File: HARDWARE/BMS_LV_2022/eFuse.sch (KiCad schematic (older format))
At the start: 12 parts, among them Q10 BSS138, Q11 SiSS05DN, Q12 SiSS05DN, Q8 SiSS05DN, Q9 SiSS05DN

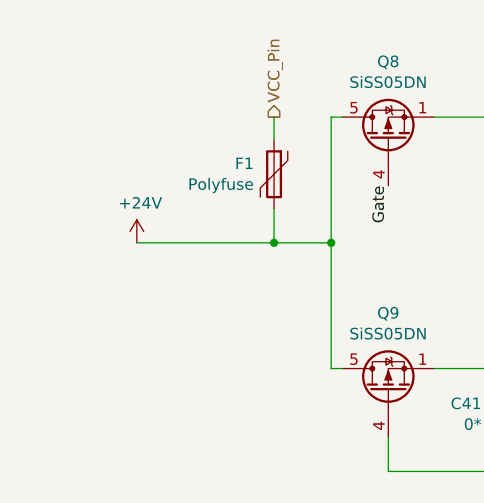
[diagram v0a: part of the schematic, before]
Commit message: PCB Routing Update 2
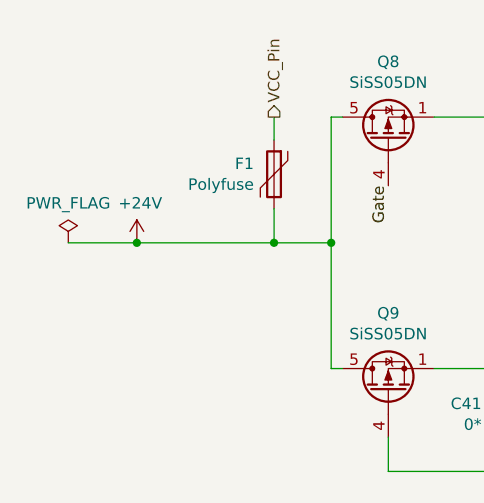
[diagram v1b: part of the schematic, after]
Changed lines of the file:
@@
 Wire Wire Line
 	6050 3350 6050 3450
+$Comp
+L power:PWR_FLAG #FLG0106
+U 1 1 61ECFB96
+P 3950 2800
+F 0 "#FLG0106" H 3950 2875 50  0001 C CNN
+F 1 "PWR_FLAG" H 3950 2973 50  0000 C CNN
+F 2 "" H 3950 2800 50  0001 C CNN
+F 3 "~" H 3950 2800 50  0001 C CNN
+	1    3950 2800
+	1    0    0    -1
+$EndComp
+Wire Wire Line
+	4250 2800 3950 2800
+Connection ~ 4250 2800
 $EndSCHEMATC

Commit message: Changes in V1.0
-Fuse holder change
-Autosport conn angle change
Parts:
- F2: footprint footprints:Fuseholder_Keystone_3522-2 -> footprints:3557-2; Part Number 3522-2 -> 3557-2
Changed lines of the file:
@@
 F 0 "F2" V 6853 2800 50  0000 C CNN
 F 1 "Fuse" V 6944 2800 50  0000 C CNN
-F 2 "footprints:Fuseholder_Keystone_3522-2" V 6980 2800 50  0001 C CNN
+F 2 "footprints:3557-2" V 6980 2800 50  0001 C CNN
 F 3 "~" H 7050 2800 50  0001 C CNN
-F 4 "3522-2" H 7050 2800 50  0001 C CNN "Part Number"
+F 4 "3557-2" H 7050 2800 50  0001 C CNN "Part Number"
 	1    7050 2800
 	0    1    1    0

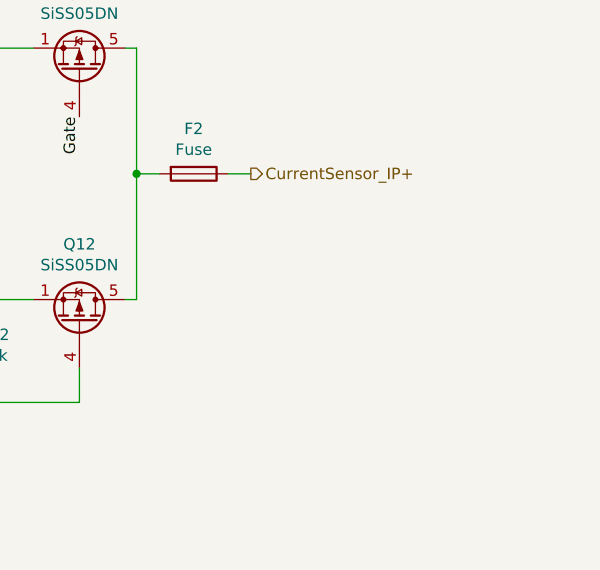
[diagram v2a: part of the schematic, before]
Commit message: Last Changes in V1.0
Fuse voltage measurement added
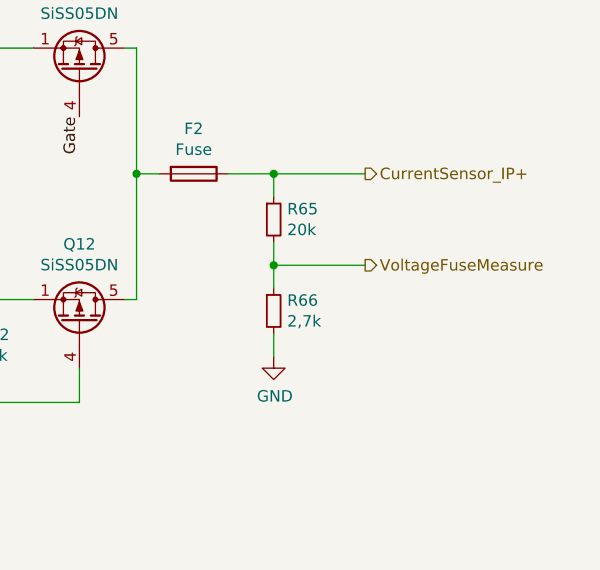
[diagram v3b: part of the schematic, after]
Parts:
- added R65: 20k, Resistor_SMD:R_0603_1608Metric, symbol Device:R_Small
- added R66: 2,7k, Resistor_SMD:R_0603_1608Metric, symbol Device:R_Small
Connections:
- net CurrentSensor_IP+: now also R65.1
- net GND: now also R66.2
- new net VoltageFuseMeasure: R65.2, R66.1
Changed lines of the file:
@@
 $Descr A4 11693 8268
 encoding utf-8
-Sheet 12 13
+Sheet 13 13
 Title "eFuse"
 Date ""
@@
 	5150 2250 5100 2250
 Wire Wire Line
-	7300 2800 7200 2800
-Wire Wire Line
 	6800 2800 6900 2800
 Wire Wire Line
@@
 Text Label 5350 2550 3    50   ~ 0
 Gate
-Text HLabel 7300 2800 2    50   Output ~ 0
+Text HLabel 7800 2800 2    50   Output ~ 0
 CurrentSensor_IP+
 Wire Wire Line
@@
 	4250 2800 3950 2800
 Connection ~ 4250 2800
+$Comp
+L Device:R_Small R65
+U 1 1 61EF9D80
+P 7400 3000
+F 0 "R65" H 7459 3046 50  0000 L CNN
+F 1 "20k" H 7459 2955 50  0000 L CNN
+F 2 "Resistor_SMD:R_0603_1608Metric" H 7400 3000 50  0001 C CNN
+F 3 "~" H 7400 3000 50  0001 C CNN
+	1    7400 3000
+	1    0    0    -1
+$EndComp
+$Comp
+L Device:R_Small R66
+U 1 1 61EFA7A0
+P 7400 3400
+F 0 "R66" H 7459 3446 50  0000 L CNN
+F 1 "2,7k" H 7459 3355 50  0000 L CNN
+F 2 "Resistor_SMD:R_0603_1608Metric" H 7400 3400 50  0001 C CNN
+F 3 "~" H 7400 3400 50  0001 C CNN
+	1    7400 3400
+	1    0    0    -1
+$EndComp
+Wire Wire Line
+	7400 2900 7400 2800
+Wire Wire Line
+	7200 2800 7400 2800
+Wire Wire Line
+	7400 3100 7400 3200
+Wire Wire Line
+	7400 3500 7400 3600
+$Comp
+L power:GND #PWR?
+U 1 1 61EFD62C
+P 7400 3600
+AR Path="/61EFD62C" Ref="#PWR?"  Part="1"
+AR Path="/6269845F/61EFD62C" Ref="#PWR0101"  Part="1"
+F 0 "#PWR0101" H 7400 3350 50  0001 C CNN
+F 1 "GND" H 7405 3427 50  0000 C CNN
+F 2 "" H 7400 3600 50  0001 C CNN
+F 3 "" H 7400 3600 50  0001 C CNN
+	1    7400 3600
+	1    0    0    -1
+$EndComp
+Wire Wire Line
+	7400 2800 7800 2800
+Connection ~ 7400 2800
+Wire Wire Line
+	7400 3200 7800 3200
+Connection ~ 7400 3200
+Wire Wire Line
+	7400 3200 7400 3300
+Text HLabel 7800 3200 2    50   Output ~ 0
+VoltageFuseMeasure
 $EndSCHEMATC
